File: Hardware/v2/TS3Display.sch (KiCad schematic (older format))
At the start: 26 parts, among them J1 Conn_01x04, J2 Conn_ARM_JTAG_SWD_10, U1 SPX3819M5-L-3-3, U2 USBLC6-2P6, U3 ATSAMD21G18A-AU, U4 NHD-2.8-240320AF-CSXP-F, U5 PAM2804, Y1 32.768k

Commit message: Use different connector for USB connection
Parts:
- added R3: 10k, Resistors_SMD:R_0805, symbol Device:R
- added SW1: SW_Push, Buttons_Switches_SMD:SW_SPST_PTS810, symbol Switch:SW_Push
- J1: value Conn_01x04 -> Conn_01x05; footprint Pin_Headers:Pin_Header_Angled_1x04_Pitch1.27mm -> Connectors_JST:JST_SH_BM05B-SRSS-TB_05x1.00mm_Straight; symbol Connector_Generic:Conn_01x04 -> Connector_Generic:Conn_01x05
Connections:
- net 3.3V: now also R3.1
- net GND: now also SW1.1
- net ~RESET: now also R3.2, SW1.2
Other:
- moved on the sheet: C1, C2, C3, J2, R2, U1
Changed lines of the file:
@@
 L Regulator_Linear:SPX3819M5-L-3-3 U1
 U 1 1 5FC94A55
-P 2250 2750
-F 0 "U1" H 2250 3092 50  0000 C CNN
-F 1 "SPX3819M5-L-3-3" H 2250 3001 50  0000 C CNN
-F 2 "TO_SOT_Packages_SMD:SOT-23-5" H 2250 3075 50  0001 C CNN
-F 3 "https://www.exar.com/content/document.ashx?id=22106&languageid=1033&type=Datasheet&partnumber=SPX3819&filename=SPX3819.pdf&part=SPX3819" H 2250 2750 50  0001 C CNN
-	1    2250 2750
-	1    0    0    -1
-$EndComp
-Wire Wire Line
-	1950 2750 1900 2750
-Wire Wire Line
-	1900 2750 1900 2650
-Wire Wire Line
-	1900 2650 1950 2650
-Wire Wire Line
-	1900 2650 1850 2650
-Connection ~ 1900 2650
-Text GLabel 1850 2650 0    50   Input ~ 0
+P 1700 2750
+F 0 "U1" H 1700 3092 50  0000 C CNN
+F 1 "SPX3819M5-L-3-3" H 1700 3001 50  0000 C CNN
+F 2 "TO_SOT_Packages_SMD:SOT-23-5" H 1700 3075 50  0001 C CNN
+F 3 "https://www.exar.com/content/document.ashx?id=22106&languageid=1033&type=Datasheet&partnumber=SPX3819&filename=SPX3819.pdf&part=SPX3819" H 1700 2750 50  0001 C CNN
+	1    1700 2750
+	1    0    0    -1
+$EndComp
+Wire Wire Line
+	1400 2750 1350 2750
+Wire Wire Line
+	1350 2750 1350 2650
+Wire Wire Line
+	1350 2650 1400 2650
+Wire Wire Line
+	1350 2650 1300 2650
+Connection ~ 1350 2650
+Text GLabel 1300 2650 0    50   Input ~ 0
 5V
 $Comp
 L Device:C C2
 U 1 1 5FCAFE5E
-P 2600 2950
-F 0 "C2" H 2485 2904 50  0000 R CNN
-F 1 "10n" H 2485 2995 50  0000 R CNN
-F 2 "Capacitors_SMD:C_0805" H 2638 2800 50  0001 C CNN
-F 3 "~" H 2600 2950 50  0001 C CNN
-	1    2600 2950
+P 2050 2950
+F 0 "C2" H 1935 2904 50  0000 R CNN
+F 1 "10n" H 1935 2995 50  0000 R CNN
+F 2 "Capacitors_SMD:C_0805" H 2088 2800 50  0001 C CNN
+F 3 "~" H 2050 2950 50  0001 C CNN
+	1    2050 2950
 	-1   0    0    1
 $EndComp
 Wire Wire Line
-	2550 2750 2600 2750
-Wire Wire Line
-	2600 2750 2600 2800
-Wire Wire Line
-	1900 2750 1900 2800
-Connection ~ 1900 2750
+	2000 2750 2050 2750
+Wire Wire Line
+	2050 2750 2050 2800
+Wire Wire Line
+	1350 2750 1350 2800
+Connection ~ 1350 2750
 $Comp
 L Device:C C3
 U 1 1 5FCC5AB9
-P 3000 2950
-F 0 "C3" H 3115 2996 50  0000 L CNN
-F 1 "10u" H 3115 2905 50  0000 L CNN
-F 2 "Capacitors_SMD:C_0805" H 3038 2800 50  0001 C CNN
-F 3 "~" H 3000 2950 50  0001 C CNN
-	1    3000 2950
-	1    0    0    -1
-$EndComp
-Wire Wire Line
-	1900 3150 2250 3150
+P 2450 2950
+F 0 "C3" H 2565 2996 50  0000 L CNN
+F 1 "10u" H 2565 2905 50  0000 L CNN
+F 2 "Capacitors_SMD:C_0805" H 2488 2800 50  0001 C CNN
+F 3 "~" H 2450 2950 50  0001 C CNN
+	1    2450 2950
+	1    0    0    -1
+$EndComp
+Wire Wire Line
+	1350 3150 1700 3150
 $Comp
 L Device:C C1
 U 1 1 5FCBA599
-P 1900 2950
-F 0 "C1" H 1650 3000 50  0000 L CNN
-F 1 "1u" H 1650 2900 50  0000 L CNN
-F 2 "Capacitors_SMD:C_0805" H 1938 2800 50  0001 C CNN
-F 3 "~" H 1900 2950 50  0001 C CNN
-	1    1900 2950
-	1    0    0    -1
-$EndComp
-Wire Wire Line
-	2250 3150 2250 3200
-Connection ~ 2250 3150
-Wire Wire Line
-	2250 3150 2600 3150
-Text GLabel 2250 3200 3    50   Input ~ 0
-GND
-Wire Wire Line
-	1900 3100 1900 3150
-Wire Wire Line
-	2250 3050 2250 3150
-Wire Wire Line
-	2600 3100 2600 3150
-Wire Wire Line
-	2600 3150 3000 3150
-Wire Wire Line
-	3000 3150 3000 3100
-Connection ~ 2600 3150
-Wire Wire Line
-	2550 2650 3000 2650
-Wire Wire Line
-	3000 2650 3000 2800
-Connection ~ 3000 2650
-Wire Wire Line
-	3000 2650 3050 2650
-Text GLabel 3050 2650 2    50   Input ~ 0
+P 1350 2950
+F 0 "C1" H 1100 3000 50  0000 L CNN
+F 1 "1u" H 1100 2900 50  0000 L CNN
+F 2 "Capacitors_SMD:C_0805" H 1388 2800 50  0001 C CNN
+F 3 "~" H 1350 2950 50  0001 C CNN
+	1    1350 2950
+	1    0    0    -1
+$EndComp
+Wire Wire Line
+	1700 3150 1700 3200
+Connection ~ 1700 3150
+Wire Wire Line
+	1700 3150 2050 3150
+Text GLabel 1700 3200 3    50   Input ~ 0
+GND
+Wire Wire Line
+	1350 3100 1350 3150
+Wire Wire Line
+	1700 3050 1700 3150
+Wire Wire Line
+	2050 3100 2050 3150
+Wire Wire Line
+	2050 3150 2450 3150
+Wire Wire Line
+	2450 3150 2450 3100
+Connection ~ 2050 3150
+Wire Wire Line
+	2000 2650 2450 2650
+Wire Wire Line
+	2450 2650 2450 2800
+Connection ~ 2450 2650
+Wire Wire Line
+	2450 2650 2500 2650
+Text GLabel 2500 2650 2    50   Input ~ 0
 3.3V
 Text GLabel 4600 3250 0    50   Input ~ 0
@@
 	8300 1300 8300 1350
 $Comp
-L Connector_Generic:Conn_01x04 J1
+L Connector_Generic:Conn_01x05 J1
 U 1 1 5FE3EB5F
-P 700 1150
-F 0 "J1" H 618 1467 50  0000 C CNN
-F 1 "Conn_01x04" H 618 1376 50  0000 C CNN
-F 2 "Pin_Headers:Pin_Header_Angled_1x04_Pitch1.27mm" H 700 1150 50  0001 C CNN
-F 3 "~" H 700 1150 50  0001 C CNN
-	1    700  1150
+P 700 1050
+F 0 "J1" H 600 1450 50  0000 C CNN
+F 1 "Conn_01x05" H 600 1350 50  0000 C CNN
+F 2 "Connectors_JST:JST_SH_BM05B-SRSS-TB_05x1.00mm_Straight" H 700 1050 50  0001 C CNN
+F 3 "~" H 700 1050 50  0001 C CNN
+	1    700  1050
 	-1   0    0    1
 $EndComp
@@
 L Connector:Conn_ARM_JTAG_SWD_10 J2
 U 1 1 5FD5D1FB
-P 2350 4650
-F 0 "J2" H 2150 5250 50  0000 R CNN
-F 1 "Conn_ARM_JTAG_SWD_10" V 2050 5100 50  0000 R CNN
-F 2 "Pin_Headers:Pin_Header_Straight_2x05_Pitch1.27mm_SMD" H 2350 4650 50  0001 C CNN
-F 3 "http://infocenter.arm.com/help/topic/com.arm.doc.ddi0314h/DDI0314H_coresight_components_trm.pdf" V 2000 3400 50  0001 C CNN
-	1    2350 4650
-	1    0    0    -1
-$EndComp
-Text GLabel 2250 5300 3    50   Input ~ 0
-GND
-Text GLabel 2350 5300 3    50   Input ~ 0
-GND
-Text GLabel 2350 4000 1    50   Input ~ 0
-3.3V
-Text GLabel 2900 4350 2    50   Input ~ 0
+P 1900 4650
+F 0 "J2" H 1700 5250 50  0000 R CNN
+F 1 "Conn_ARM_JTAG_SWD_10" V 1600 5100 50  0000 R CNN
+F 2 "Pin_Headers:Pin_Header_Straight_2x05_Pitch1.27mm_SMD" H 1900 4650 50  0001 C CNN
+F 3 "http://infocenter.arm.com/help/topic/com.arm.doc.ddi0314h/DDI0314H_coresight_components_trm.pdf" V 1550 3400 50  0001 C CNN
+	1    1900 4650
+	1    0    0    -1
+$EndComp
+Text GLabel 1800 5300 3    50   Input ~ 0
+GND
+Text GLabel 1900 5300 3    50   Input ~ 0
+GND
+Text GLabel 1900 4000 1    50   Input ~ 0
+3.3V
+Text GLabel 2450 4350 2    50   Input ~ 0
 ~RESET
 Text GLabel 4600 2350 0    50   Input ~ 0
@@
 	4600 2350 4650 2350
 Wire Wire Line
-	2850 4350 2900 4350
-Text GLabel 2900 4650 2    50   Input ~ 0
+	2400 4350 2450 4350
+Text GLabel 2450 4650 2    50   Input ~ 0
 SWDIO
-Text GLabel 2900 4550 2    50   Input ~ 0
+Text GLabel 2450 4550 2    50   Input ~ 0
 SWDCLK
 Text GLabel 4600 5450 0    50   Input ~ 0
@@
 SWDIO
 Wire Wire Line
-	2850 4550 2900 4550
-Wire Wire Line
-	2850 4650 2900 4650
-Wire Wire Line
-	2350 4000 2350 4050
-Wire Wire Line
-	2250 5250 2250 5300
-Wire Wire Line
-	2350 5250 2350 5300
+	2400 4550 2450 4550
+Wire Wire Line
+	2400 4650 2450 4650
+Wire Wire Line
+	1900 4000 1900 4050
+Wire Wire Line
+	1800 5250 1800 5300
+Wire Wire Line
+	1900 5250 1900 5300
 Wire Wire Line
 	4600 5450 4650 5450
@@
 L Device:R R2
 U 1 1 5FDA6B25
-P 1700 4550
-F 0 "R2" H 1770 4596 50  0000 L CNN
-F 1 "10k" H 1770 4505 50  0000 L CNN
-F 2 "Resistors_SMD:R_0805" V 1630 4550 50  0001 C CNN
-F 3 "~" H 1700 4550 50  0001 C CNN
-	1    1700 4550
-	1    0    0    -1
-$EndComp
-Text GLabel 1700 4750 3    50   Input ~ 0
+P 1250 4550
+F 0 "R2" H 1320 4596 50  0000 L CNN
+F 1 "10k" H 1320 4505 50  0000 L CNN
+F 2 "Resistors_SMD:R_0805" V 1180 4550 50  0001 C CNN
+F 3 "~" H 1250 4550 50  0001 C CNN
+	1    1250 4550
+	1    0    0    -1
+$EndComp
+Text GLabel 1250 4750 3    50   Input ~ 0
 SWDCLK
-Text GLabel 1700 4350 1    50   Input ~ 0
-3.3V
-Wire Wire Line
-	1700 4350 1700 4400
-Wire Wire Line
-	1700 4700 1700 4750
+Text GLabel 1250 4350 1    50   Input ~ 0
+3.3V
+Wire Wire Line
+	1250 4350 1250 4400
+Wire Wire Line
+	1250 4700 1250 4750
+$Comp
+L Switch:SW_Push SW1
+U 1 1 603D339B
+P 3300 3800
+F 0 "SW1" V 3346 3752 50  0000 R CNN
+F 1 "SW_Push" V 3255 3752 50  0000 R CNN
+F 2 "Buttons_Switches_SMD:SW_SPST_PTS810" H 3300 4000 50  0001 C CNN
+F 3 "~" H 3300 4000 50  0001 C CNN
+	1    3300 3800
+	0    -1   -1   0
+$EndComp
+$Comp
+L Device:R R3
+U 1 1 603D5250
+P 3300 3350
+F 0 "R3" H 3370 3396 50  0000 L CNN
+F 1 "10k" H 3370 3305 50  0000 L CNN
+F 2 "Resistors_SMD:R_0805" V 3230 3350 50  0001 C CNN
+F 3 "~" H 3300 3350 50  0001 C CNN
+	1    3300 3350
+	1    0    0    -1
+$EndComp
+Text GLabel 3300 4050 3    50   Input ~ 0
+GND
+Text GLabel 3250 3550 0    50   Input ~ 0
+~RESET
+Text GLabel 3300 3150 1    50   Input ~ 0
+3.3V
+Wire Wire Line
+	3300 3150 3300 3200
+Wire Wire Line
+	3300 3500 3300 3550
+Wire Wire Line
+	3250 3550 3300 3550
+Connection ~ 3300 3550
+Wire Wire Line
+	3300 3550 3300 3600
+Wire Wire Line
+	3300 4000 3300 4050
 $EndSCHEMATC

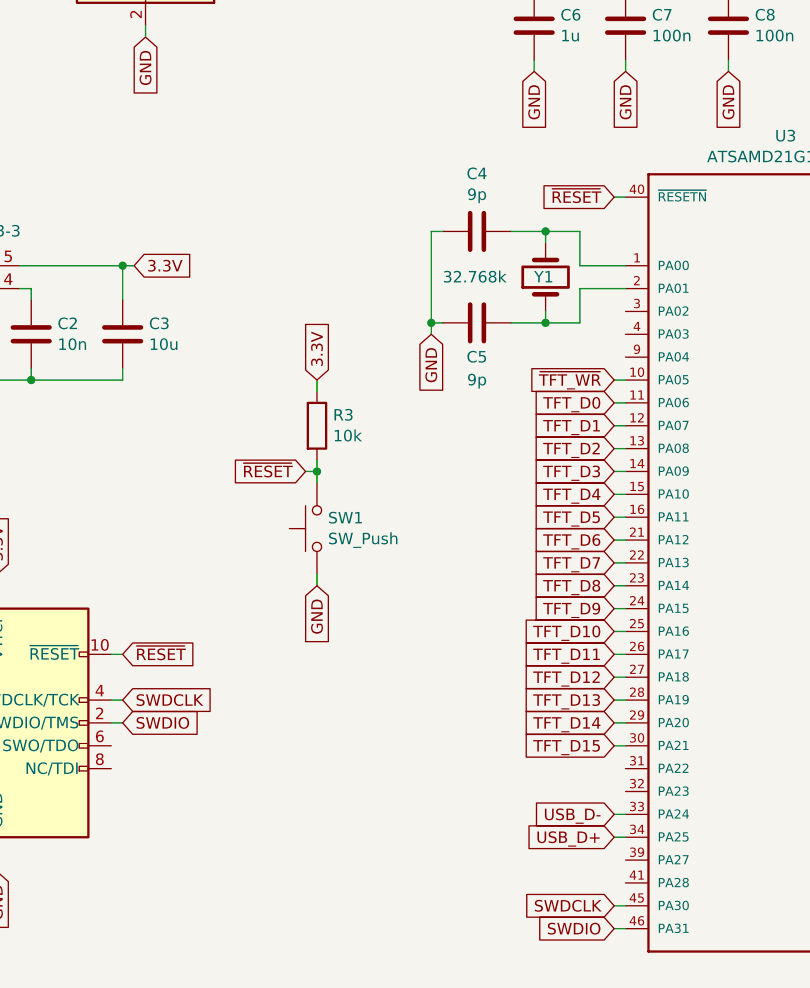
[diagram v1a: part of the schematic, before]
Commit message: Fix crystal connections
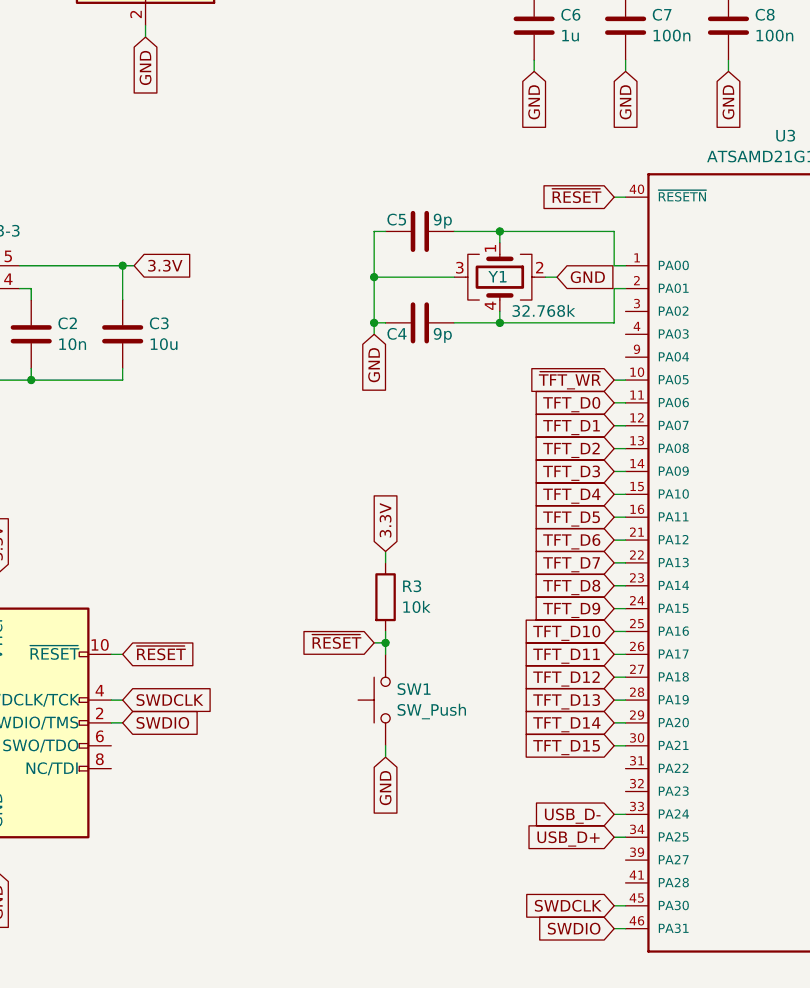
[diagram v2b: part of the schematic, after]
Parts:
- removed Y1: 32.768k, Crystals:Crystal_SMD_SeikoEpson_MC146-4pin_6.7x1.5mm, symbol Device:Crystal
- added Y1: 32.768k, Crystals:Crystal_SMD_SeikoEpson_MC146-4pin_6.7x1.5mm, symbol Device:Crystal_GND23
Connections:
- net GND: now also Y1.2, Y1.3
- net at U3.1 (PA00): now also C5.1, Y1.1; no longer C4.1
- net at U3.2 (PA01): now also C4.1, Y1.4; no longer C5.1
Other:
- moved on the sheet: C4, C5, R3, SW1
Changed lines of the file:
@@
 Wire Wire Line
 	6050 3850 6100 3850
-$Comp
-L Device:Crystal Y1
-U 1 1 5FBA811F
-P 4300 2700
-F 0 "Y1" V 4300 2750 50  0000 R CNN
-F 1 "32.768k" V 4300 3150 50  0000 R CNN
-F 2 "Crystals:Crystal_SMD_SeikoEpson_MC146-4pin_6.7x1.5mm" H 4300 2700 50  0001 C CNN
-F 3 "~" H 4300 2700 50  0001 C CNN
-	1    4300 2700
-	0    -1   -1   0
-$EndComp
-Wire Wire Line
-	4450 2750 4650 2750
-Wire Wire Line
-	4450 2650 4650 2650
+Wire Wire Line
+	4600 2750 4650 2750
+Wire Wire Line
+	4600 2650 4650 2650
 $Comp
 L Device:C C4
 U 1 1 5FBAC4E5
-P 4000 2500
-F 0 "C4" V 3748 2500 50  0000 C CNN
-F 1 "9p" V 3839 2500 50  0000 C CNN
-F 2 "Capacitors_SMD:C_0805" H 4038 2350 50  0001 C CNN
-F 3 "~" H 4000 2500 50  0001 C CNN
-	1    4000 2500
+P 3750 2900
+F 0 "C4" V 3800 2800 50  0000 C CNN
+F 1 "9p" V 3800 3000 50  0000 C CNN
+F 2 "Capacitors_SMD:C_0805" H 3788 2750 50  0001 C CNN
+F 3 "~" H 3750 2900 50  0001 C CNN
+	1    3750 2900
 	0    1    1    0
 $EndComp
@@
 L Device:C C5
 U 1 1 5FBADD6A
-P 4000 2900
-F 0 "C5" V 4150 2900 50  0000 C CNN
-F 1 "9p" V 4250 2900 50  0000 C CNN
-F 2 "Capacitors_SMD:C_0805" H 4038 2750 50  0001 C CNN
-F 3 "~" H 4000 2900 50  0001 C CNN
-	1    4000 2900
+P 3750 2500
+F 0 "C5" V 3700 2400 50  0000 C CNN
+F 1 "9p" V 3700 2600 50  0000 C CNN
+F 2 "Capacitors_SMD:C_0805" H 3788 2350 50  0001 C CNN
+F 3 "~" H 3750 2500 50  0001 C CNN
+	1    3750 2500
 	0    1    1    0
 $EndComp
 Wire Wire Line
-	4300 2550 4300 2500
-Wire Wire Line
-	4300 2500 4450 2500
-Wire Wire Line
-	4450 2500 4450 2650
-Wire Wire Line
-	4300 2850 4300 2900
-Wire Wire Line
-	4300 2900 4450 2900
-Wire Wire Line
-	4450 2750 4450 2900
-Wire Wire Line
-	4300 2900 4150 2900
-Connection ~ 4300 2900
-Wire Wire Line
-	4300 2500 4150 2500
-Connection ~ 4300 2500
-Wire Wire Line
-	3850 2500 3800 2500
-Wire Wire Line
-	3800 2500 3800 2900
-Wire Wire Line
-	3850 2900 3800 2900
-Connection ~ 3800 2900
-Wire Wire Line
-	3800 2900 3800 2950
-Text GLabel 3800 2950 3    50   Input ~ 0
+	4600 2500 4600 2650
+Wire Wire Line
+	4600 2750 4600 2900
+Wire Wire Line
+	3600 2500 3550 2500
+Text GLabel 3550 2950 3    50   Input ~ 0
 GND
 Wire Wire Line
@@
 L Switch:SW_Push SW1
 U 1 1 603D339B
-P 3300 3800
-F 0 "SW1" V 3346 3752 50  0000 R CNN
-F 1 "SW_Push" V 3255 3752 50  0000 R CNN
-F 2 "Buttons_Switches_SMD:SW_SPST_PTS810" H 3300 4000 50  0001 C CNN
-F 3 "~" H 3300 4000 50  0001 C CNN
-	1    3300 3800
+P 3600 4550
+F 0 "SW1" V 3646 4502 50  0000 R CNN
+F 1 "SW_Push" V 3555 4502 50  0000 R CNN
+F 2 "Buttons_Switches_SMD:SW_SPST_PTS810" H 3600 4750 50  0001 C CNN
+F 3 "~" H 3600 4750 50  0001 C CNN
+	1    3600 4550
 	0    -1   -1   0
 $EndComp
@@
 L Device:R R3
 U 1 1 603D5250
-P 3300 3350
-F 0 "R3" H 3370 3396 50  0000 L CNN
-F 1 "10k" H 3370 3305 50  0000 L CNN
-F 2 "Resistors_SMD:R_0805" V 3230 3350 50  0001 C CNN
-F 3 "~" H 3300 3350 50  0001 C CNN
-	1    3300 3350
-	1    0    0    -1
-$EndComp
-Text GLabel 3300 4050 3    50   Input ~ 0
-GND
-Text GLabel 3250 3550 0    50   Input ~ 0
+P 3600 4100
+F 0 "R3" H 3670 4146 50  0000 L CNN
+F 1 "10k" H 3670 4055 50  0000 L CNN
+F 2 "Resistors_SMD:R_0805" V 3530 4100 50  0001 C CNN
+F 3 "~" H 3600 4100 50  0001 C CNN
+	1    3600 4100
+	1    0    0    -1
+$EndComp
+Text GLabel 3600 4800 3    50   Input ~ 0
+GND
+Text GLabel 3550 4300 0    50   Input ~ 0
 ~RESET
-Text GLabel 3300 3150 1    50   Input ~ 0
-3.3V
-Wire Wire Line
-	3300 3150 3300 3200
-Wire Wire Line
-	3300 3500 3300 3550
-Wire Wire Line
-	3250 3550 3300 3550
-Connection ~ 3300 3550
-Wire Wire Line
-	3300 3550 3300 3600
-Wire Wire Line
-	3300 4000 3300 4050
+Text GLabel 3600 3900 1    50   Input ~ 0
+3.3V
+Wire Wire Line
+	3600 3900 3600 3950
+Wire Wire Line
+	3600 4250 3600 4300
+Wire Wire Line
+	3550 4300 3600 4300
+Connection ~ 3600 4300
+Wire Wire Line
+	3600 4300 3600 4350
+Wire Wire Line
+	3600 4750 3600 4800
+$Comp
+L Device:Crystal_GND23 Y1
+U 1 1 6075063B
+P 4100 2700
+F 0 "Y1" V 4100 2650 50  0000 L CNN
+F 1 "32.768k" V 4250 2750 50  0000 L CNN
+F 2 "Crystals:Crystal_SMD_SeikoEpson_MC146-4pin_6.7x1.5mm" H 4100 2700 50  0001 C CNN
+F 3 "~" H 4100 2700 50  0001 C CNN
+	1    4100 2700
+	0    1    1    0
+$EndComp
+Wire Wire Line
+	3900 2500 4100 2500
+Wire Wire Line
+	3900 2900 4100 2900
+Wire Wire Line
+	4100 2850 4100 2900
+Connection ~ 4100 2900
+Wire Wire Line
+	4100 2900 4600 2900
+Wire Wire Line
+	4100 2550 4100 2500
+Connection ~ 4100 2500
+Wire Wire Line
+	4100 2500 4600 2500
+Text GLabel 4350 2700 2    50   Input ~ 0
+GND
+Wire Wire Line
+	3550 2900 3550 2950
+Wire Wire Line
+	3600 2900 3550 2900
+Connection ~ 3550 2700
+Wire Wire Line
+	3900 2700 3550 2700
+Connection ~ 3550 2900
+Wire Wire Line
+	3550 2500 3550 2700
+Wire Wire Line
+	3550 2700 3550 2900
+Wire Wire Line
+	4300 2700 4350 2700
 $EndSCHEMATC
